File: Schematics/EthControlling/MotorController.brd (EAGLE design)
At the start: 90 x 80 mm, 114 parts, among them IC1 TLP621-2, IC2 MEGA164P/324P/644P-AU, IC3 OPA4234P, IC4 TLP621-2, Q1 20.000M, T1 2SC1815, T2 2SC1815, T3 2SC1815, T4 2SC1815

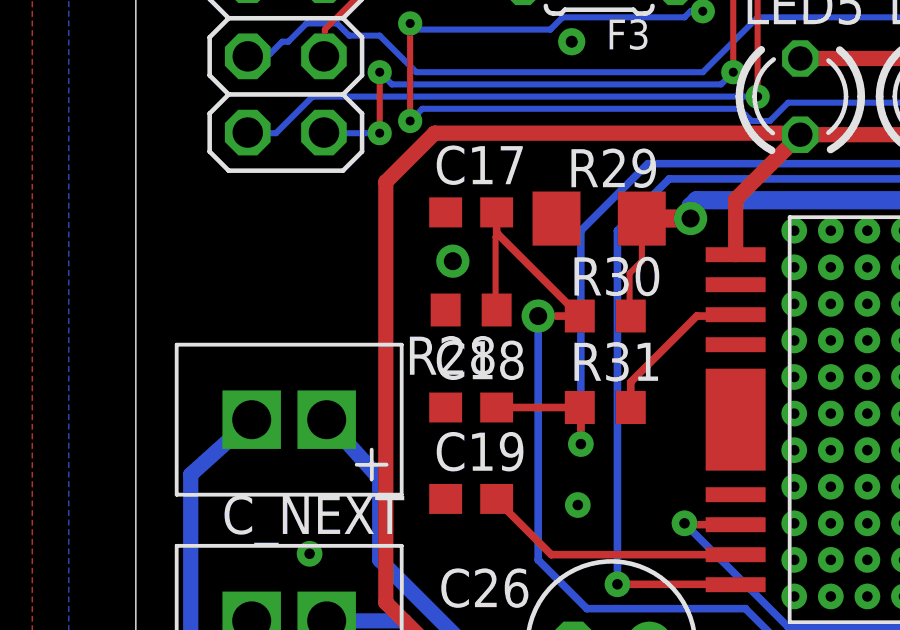
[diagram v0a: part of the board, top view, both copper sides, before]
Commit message: identify schematics by the order number on schematics and submitted gerber files
Signed-off-by: sosoru <siva6991@yahoo.co.jp>
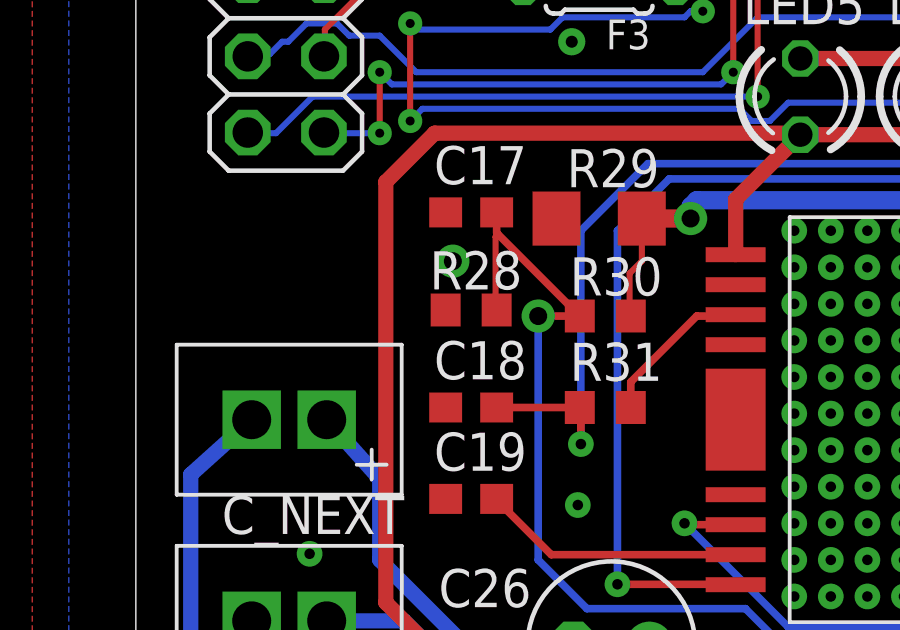
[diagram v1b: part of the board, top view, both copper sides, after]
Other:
- board text added: "D53371"
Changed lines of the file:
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@@
 <rectangle x1="78.28915" y1="53.80355" x2="78.36535" y2="53.84165" layer="26" rot="R180"/>
 <rectangle x1="78.28915" y1="53.99405" x2="78.32725" y2="54.03215" layer="26" rot="R180"/>
+<text x="9.3472" y="70.3072" size="1.778" layer="26" rot="MR0">D53371</text>
 </plain>
 <attributes>
@@
 <attribute name="VALUE" x="35.0266" y="57.912" size="1.27" layer="27" rot="R180"/>
 </element>
-<element name="R28" library="resistor" package="R0603" value="1Meg" x="11.176" y="25.1968" rot="R180"/>
+<element name="R28" library="resistor" package="R0603" value="1Meg" x="11.176" y="25.1968" smashed="yes" rot="R180">
+<attribute name="NAME" x="12.8778" y="27.1526" size="1.27" layer="25" rot="R180"/>
+<attribute name="VALUE" x="12.065" y="27.2288" size="1.27" layer="27" rot="R180"/>
+</element>
 <element name="R34" library="resistor" package="R0603" value="1Meg" x="56.0832" y="22.9616" smashed="yes" rot="R180">
 <attribute name="NAME" x="57.785" y="24.9174" size="1.27" layer="25" font="vector" rot="R180"/>

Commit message: fix resistor value of MotorController
Signed-off-by: sosoru <siva6991@yahoo.co.jp>
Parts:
- R18, R20, R24, R27: value 25k -> 33k
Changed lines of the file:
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@@
 <attribute name="VALUE" x="77.7494" y="47.3456" size="1.27" layer="27" font="vector"/>
 </element>
-<element name="R20" library="resistor" package="R0603" value="25k" x="78.6384" y="46.1264" smashed="yes">
+<element name="R20" library="resistor" package="R0603" value="33k" x="78.6384" y="46.1264" smashed="yes">
 <attribute name="NAME" x="76.9366" y="47.0154" size="1.27" layer="25" font="vector"/>
 <attribute name="VALUE" x="77.7494" y="44.0944" size="1.27" layer="27" font="vector"/>
@@
 <attribute name="VALUE" x="78.3082" y="33.3248" size="1.27" layer="27" font="vector" rot="R180"/>
 </element>
-<element name="R27" library="resistor" package="R0603" value="25k" x="81.8896" y="31.2928" smashed="yes">
+<element name="R27" library="resistor" package="R0603" value="33k" x="81.8896" y="31.2928" smashed="yes">
 <attribute name="NAME" x="80.391" y="32.1818" size="1.27" layer="25" font="vector"/>
 <attribute name="VALUE" x="81.0006" y="29.2608" size="1.27" layer="27" font="vector"/>
@@
 <attribute name="VALUE" x="74.6506" y="51.4096" size="1.27" layer="27" font="vector" rot="R180"/>
 </element>
-<element name="R18" library="resistor" package="R0603" value="25k" x="73.7616" y="46.1264" smashed="yes" rot="R180">
+<element name="R18" library="resistor" package="R0603" value="33k" x="73.7616" y="46.1264" smashed="yes" rot="R180">
 <attribute name="NAME" x="75.6666" y="48.2854" size="1.27" layer="25" font="vector" rot="R180"/>
 <attribute name="VALUE" x="74.6506" y="48.1584" size="1.27" layer="27" font="vector" rot="R180"/>
@@
 <attribute name="VALUE" x="72.4662" y="29.2608" size="1.27" layer="27" font="vector"/>
 </element>
-<element name="R24" library="resistor" package="R0603" value="25k" x="69.088" y="31.2928" smashed="yes" rot="R180">
+<element name="R24" library="resistor" package="R0603" value="33k" x="69.088" y="31.2928" smashed="yes" rot="R180">
 <attribute name="NAME" x="70.993" y="33.2486" size="1.27" layer="25" font="vector" rot="R180"/>
 <attribute name="VALUE" x="69.977" y="33.3248" size="1.27" layer="27" font="vector" rot="R180"/>
